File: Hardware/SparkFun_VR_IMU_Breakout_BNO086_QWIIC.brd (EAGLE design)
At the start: 30.5 x 25.4 mm, 97 parts, among them J2 SMD, J3 PTH, J4 SMD, J6 SPI, U2 BNO080, Y1 32.768kHz

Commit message: some more final changes
-added name to revisioner on sch and brd
-moved sch section names to symbol layer, added IMU name
-fixed two DRC errors (angle and stub)
-added more GND vias
-Axis labels - break linear line to show rotation line going over
-Larger SFE flame logo
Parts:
- LOGO4: value SFE_LOGO_FLAME.1_INCH -> SFE_LOGO_FLAME.2_INCH; device SparkFun-Aesthetics:SFE_LOGO_FLAME_.1 -> SparkFun-Aesthetics:SFE_LOGO_FLAME_.2
- moved LOGO4 1.60 mm to (20.4, 12.3)
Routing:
- net GND: vias 10 -> 23
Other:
- board text added: "A. England, P. Lewis"
- board text removed: "A. England"
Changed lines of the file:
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@@
 <setting verticaltext="up"/>
 </settings>
-<grid distance="0.05" unitdist="inch" unit="inch" style="lines" multiple="1" display="yes" altdistance="0.005" altunitdist="inch" altunit="inch"/>
+<grid distance="0.05" unitdist="inch" unit="inch" style="lines" multiple="1" display="yes" altdistance="0.0001" altunitdist="inch" altunit="inch"/>
 <layers>
 <layer number="1" name="Top" color="4" fill="1" visible="yes" active="yes"/>
@@
 <layer number="45" name="Holes" color="7" fill="1" visible="yes" active="yes"/>
 <layer number="46" name="Milling" color="3" fill="1" visible="no" active="yes"/>
-<layer number="47" name="Measures" color="7" fill="1" visible="yes" active="yes"/>
+<layer number="47" name="Measures" color="7" fill="1" visible="no" active="yes"/>
 <layer number="48" name="Document" color="7" fill="1" visible="no" active="yes"/>
 <layer number="49" name="Reference" color="7" fill="1" visible="yes" active="yes"/>
@@
 <layer number="98" name="Guide" color="6" fill="1" visible="no" active="no"/>
 <layer number="99" name="SpiceOrder" color="7" fill="1" visible="no" active="no"/>
-<layer number="100" name="Muster" color="7" fill="1" visible="yes" active="yes"/>
+<layer number="100" name="Muster" color="7" fill="1" visible="no" active="yes"/>
 <layer number="101" name="Patch_Top" color="12" fill="4" visible="no" active="yes"/>
 <layer number="102" name="Vscore" color="7" fill="1" visible="no" active="yes"/>
@@
 <wire x1="4.0132" y1="18.3642" x2="3.3782" y2="18.9992" width="0.1778" layer="22"/>
 <wire x1="3.3782" y1="18.3642" x2="4.0132" y2="18.9992" width="0.1778" layer="22"/>
-<wire x1="3.683" y1="17.145" x2="1.778" y2="17.145" width="0.1778" layer="21"/>
+<wire x1="3.683" y1="17.145" x2="3.159759375" y2="17.145" width="0.1778" layer="21"/>
 <wire x1="3.683" y1="17.145" x2="3.302" y2="17.526" width="0.1778" layer="21"/>
 <wire x1="3.683" y1="17.145" x2="3.302" y2="16.764" width="0.1778" layer="21"/>
@@
 <wire x1="2.667" y1="16.383" x2="2.413" y2="16.51" width="0.1778" layer="21"/>
 <wire x1="2.413" y1="16.51" x2="2.54" y2="16.764" width="0.1778" layer="21"/>
-<wire x1="1.778" y1="19.558" x2="1.778" y2="17.653" width="0.1778" layer="21"/>
+<wire x1="1.778" y1="19.558" x2="1.778" y2="19.034759375" width="0.1778" layer="21"/>
 <wire x1="1.778" y1="19.558" x2="1.397" y2="19.177" width="0.1778" layer="21"/>
 <wire x1="1.778" y1="19.558" x2="2.159" y2="19.177" width="0.1778" layer="21"/>
@@
 <wire x1="3.128778125" y1="19.656828125" x2="3.038975" y2="19.38741875" width="0.1778" layer="21"/>
 <wire x1="3.038975" y1="19.38741875" x2="3.308384375" y2="19.297615625" width="0.1778" layer="21"/>
-<wire x1="1.778" y1="19.558" x2="1.778" y2="17.653" width="0.1778" layer="22"/>
+<wire x1="1.778" y1="19.558" x2="1.778" y2="19.034759375" width="0.1778" layer="22"/>
 <wire x1="1.778" y1="19.558" x2="2.159" y2="19.177" width="0.1778" layer="22"/>
 <wire x1="1.778" y1="19.558" x2="1.397" y2="19.177" width="0.1778" layer="22"/>
@@
 <wire x1="1.016" y1="18.542" x2="1.143" y2="18.288" width="0.1778" layer="22"/>
 <wire x1="1.143" y1="18.288" x2="1.397" y2="18.415" width="0.1778" layer="22"/>
-<wire x1="3.683" y1="17.145" x2="1.778" y2="17.145" width="0.1778" layer="22"/>
+<wire x1="3.683" y1="17.145" x2="3.159759375" y2="17.145" width="0.1778" layer="22"/>
 <wire x1="3.683" y1="17.145" x2="3.302" y2="16.764" width="0.1778" layer="22"/>
 <wire x1="3.683" y1="17.145" x2="3.302" y2="17.526" width="0.1778" layer="22"/>
@@
 <dimension x1="6.35" y1="1.27" x2="6.35" y2="24.13" x3="-11.43" y3="12.7" textsize="1.27" textratio="15" layer="47" dtype="vertical" unit="inch"/>
 <dimension x1="8.89" y1="19.05" x2="8.89" y2="24.13" x3="-1.27" y3="21.59" textsize="1.27" textratio="15" layer="47" dtype="vertical" unit="inch"/>
-<text x="17.78" y="-10.16" size="1.778" layer="51" font="vector">A. England</text>
+<text x="17.78" y="-10.16" size="1.778" layer="51" font="vector">A. England, P. Lewis</text>
 <dimension x1="0" y1="25.4" x2="30.48" y2="25.4" x3="15.24" y3="35.56" textsize="1.27" textratio="15" layer="47" unit="inch"/>
 <text x="47.498" y="44.069" size="1.778" layer="51" font="vector" align="top-left">Soldermask: Red
@@
 <dimension x1="30.48" y1="0" x2="27.559" y2="18.288" x3="38.1" y3="9.144" textsize="1.27" textratio="15" layer="47" dtype="vertical" unit="inch"/>
 <dimension x1="0" y1="0" x2="5.08" y2="12.7" x3="-7.62" y3="6.35" textsize="1.27" textratio="15" layer="47" dtype="vertical" unit="inch"/>
+<wire x1="1.780540625" y1="18.552159375" x2="1.780540625" y2="17.678396875" width="0.1778" layer="21"/>
+<wire x1="1.780540625" y1="18.552159375" x2="1.780540625" y2="17.678396875" width="0.1778" layer="22"/>
+<wire x1="1.8161" y1="17.139921875" x2="2.6898625" y2="17.139921875" width="0.1778" layer="21"/>
+<wire x1="1.8161" y1="17.139921875" x2="2.6898625" y2="17.139921875" width="0.1778" layer="22"/>
 </plain>
 <attributes>
@@
 <attribute name="VALUE" x="13.462" y="16.51" size="0.6096" layer="27" font="vector" ratio="20" rot="R90" align="top-center"/>
 </element>
-<element name="LOGO4" library="SparkFun-Aesthetics" package="SFE_LOGO_FLAME_.1" value="SFE_LOGO_FLAME.1_INCH" x="19.431" y="11.049" smashed="yes"/>
+<element name="LOGO4" library="SparkFun-Aesthetics" package="SFE_LOGO_FLAME_.2" value="SFE_LOGO_FLAME.2_INCH" x="20.40128125" y="12.316459375" smashed="yes"/>
 <element name="LOGO5" library="SparkFun-Aesthetics" package="SFE_LOGO_NAME_FLAME_.1" value="SFE_LOGO_NAME_FLAME.1_INCH" x="15.181578125" y="7.642859375" smashed="yes" rot="MR0"/>
 <element name="PWR" library="SparkFun-LED" package="LED-0603" value="RED" x="27.559" y="18.288" smashed="yes" rot="R270">
@@
 <wire x1="10.16" y1="13.55" x2="10.834" y2="13.55" width="0.1524" layer="1"/>
 <wire x1="13.49" y1="14.4" x2="13.49" y2="13.815" width="0.1524" layer="1"/>
-<wire x1="12.844" y1="12.954" x2="12.84" y2="12.95" width="0.1524" layer="1"/>
 <wire x1="10.16" y1="13.55" x2="8.89" y2="13.55" width="0.1524" layer="1"/>
 <wire x1="8.89" y1="13.55" x2="6.692" y2="13.55" width="0.1524" layer="1"/>
@@
 <wire x1="23.202" y1="6.77" x2="23.241" y2="6.731" width="0.1524" layer="1"/>
 <wire x1="5.9436" y1="6.35" x2="5.9436" y2="8.89" width="0.1524" layer="16"/>
-<wire x1="5.9436" y1="8.89" x2="5.9" y2="9.71" width="0.1524" layer="16"/>
-<wire x1="5.9" y1="9.71" x2="7.62" y2="11.43" width="0.1524" layer="16"/>
 <via x="7.62" y="11.43" extent="1-16" drill="0.3048"/>
 <wire x1="7.62" y1="11.43" x2="8.382" y2="11.43" width="0.1524" layer="1"/>
@@
 <contactref element="J2" pad="2"/>
 <contactref element="J3" pad="2"/>
+<wire x1="5.9436" y1="8.89" x2="5.9436" y2="9.7536" width="0.1524" layer="16"/>
+<wire x1="5.9436" y1="9.7536" x2="7.62" y2="11.43" width="0.1524" layer="16"/>
 </signal>
 <signal name="GND">
@@
 <contactref element="J2" pad="1"/>
 <contactref element="J3" pad="1"/>
+<via x="22.733" y="10.16" extent="1-16" drill="0.3048"/>
+<via x="21.082" y="9.398" extent="1-16" drill="0.3048"/>
+<via x="19.431" y="9.652" extent="1-16" drill="0.3048"/>
+<via x="21.082" y="5.715" extent="1-16" drill="0.3048"/>
+<via x="19.431" y="5.715" extent="1-16" drill="0.3048"/>
+<via x="7.09168125" y="17.205959375" extent="1-16" drill="0.3048"/>
+<via x="5.68198125" y="17.3482" extent="1-16" drill="0.3048"/>
+<via x="3.79221875" y="17.69871875" extent="1-16" drill="0.3048"/>
+<via x="10.2209625" y="21.493478125" extent="1-16" drill="0.3048"/>
+<via x="25.27808125" y="21.4376" extent="1-16" drill="0.3048"/>
+<via x="9.667240625" y="5.323840625" extent="1-16" drill="0.3048"/>
+<via x="7.680959375" y="4.68121875" extent="1-16" drill="0.3048"/>
+<via x="4.97331875" y="4.132578125" extent="1-16" drill="0.3048"/>
 </signal>
 <signal name="CAP">
@@
 <wire x1="9.691" y1="11.85" x2="8.636" y2="10.795" width="0.1524" layer="1"/>
 <wire x1="8.636" y1="10.795" x2="6.985" y2="10.795" width="0.1524" layer="1"/>
-<wire x1="6.985" y1="10.795" x2="3.81" y2="7.62" width="0.1524" layer="1"/>
+<wire x1="6.985" y1="10.795" x2="6.35" y2="10.16" width="0.1524" layer="1"/>
+<wire x1="6.35" y1="10.16" x2="3.81" y2="7.62" width="0.1524" layer="1"/>
 <wire x1="3.81" y1="7.62" x2="1.27" y2="7.62" width="0.1524" layer="1"/>
 </signal>
@@
 <wire x1="21.59" y1="24.13" x2="20.32" y2="22.86" width="0.1524" layer="16"/>
 <wire x1="5.08" y1="5.461" x2="5.461" y2="5.08" width="0.1524" layer="16"/>
-<wire x1="5.08" y1="21.59" x2="5.08" y2="5.461" width="0.1524" layer="16"/>
-<wire x1="20.32" y1="22.86" x2="6.35" y2="22.86" width="0.1524" layer="16"/>
-<wire x1="6.35" y1="22.86" x2="5.08" y2="21.59" width="0.1524" layer="16"/>
+<wire x1="5.08" y1="21.122640625" x2="5.08" y2="5.461" width="0.1524" layer="16"/>
+<wire x1="20.32" y1="22.86" x2="6.817359375" y2="22.86" width="0.1524" layer="16"/>
+<wire x1="6.817359375" y1="22.86" x2="5.08" y2="21.122640625" width="0.1524" layer="16"/>
 <contactref element="J8" pad="2"/>
 <wire x1="6.35" y1="5.08" x2="6.35" y2="1.27" width="0.1524" layer="16"/>
@@
 <wire x1="16.99" y1="9.553" x2="17.018" y2="9.525" width="0.1524" layer="1"/>
 <via x="17.018" y="9.525" extent="1-16" drill="0.3048"/>
-<wire x1="17.018" y1="9.525" x2="17.018" y2="5.842" width="0.1524" layer="16"/>
-<wire x1="17.018" y1="5.842" x2="17.78" y2="5.08" width="0.1524" layer="16"/>
-<via x="17.78" y="5.08" extent="1-16" drill="0.3048"/>
-<wire x1="17.78" y1="5.08" x2="20.32" y2="5.08" width="0.1524" layer="1"/>
-<wire x1="20.32" y1="5.08" x2="24.13" y2="1.27" width="0.1524" layer="1"/>
+<wire x1="17.018" y1="9.525" x2="17.018" y2="5.798821875" width="0.1524" layer="16"/>
+<wire x1="17.018" y1="5.798821875" x2="17.78" y2="5.036821875" width="0.1524" layer="16"/>
+<via x="17.78" y="5.036821875" extent="1-16" drill="0.3048"/>
+<wire x1="17.78" y1="5.036821875" x2="20.363178125" y2="5.036821875" width="0.1524" layer="1"/>
+<wire x1="20.363178125" y1="5.036821875" x2="24.13" y2="1.27" width="0.1524" layer="1"/>
 </signal>
 <signal name="SCL/SCK/RX">

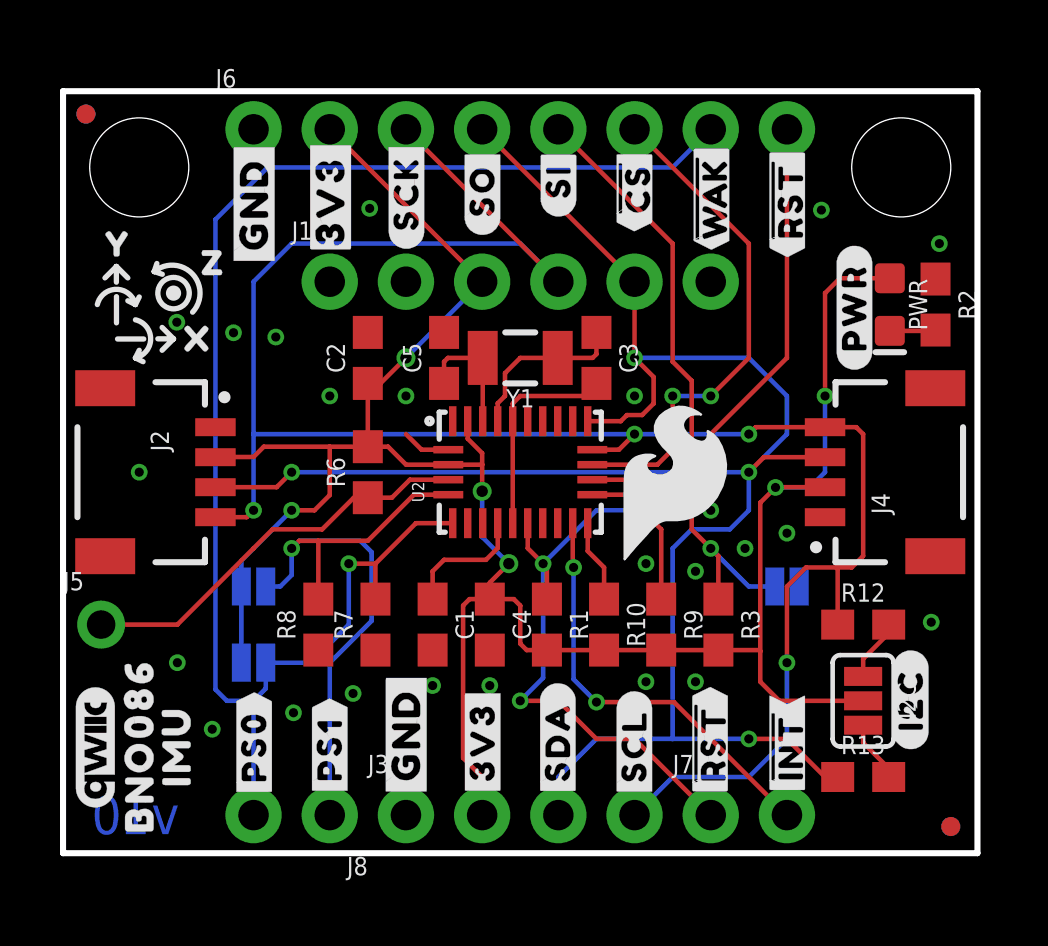
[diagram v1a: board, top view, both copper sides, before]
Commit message: 3V3 net to thicker trace and more
-upped 3v3 trace to 20mil
-nudges some vias/traces for better GND flow
-added more gnd vias
-reduced GND pour isolates from 12 to 10
-I2C pullup jumper changes to NC trace
-updated IC to 086, in temp library for now
-added Power LED jumper
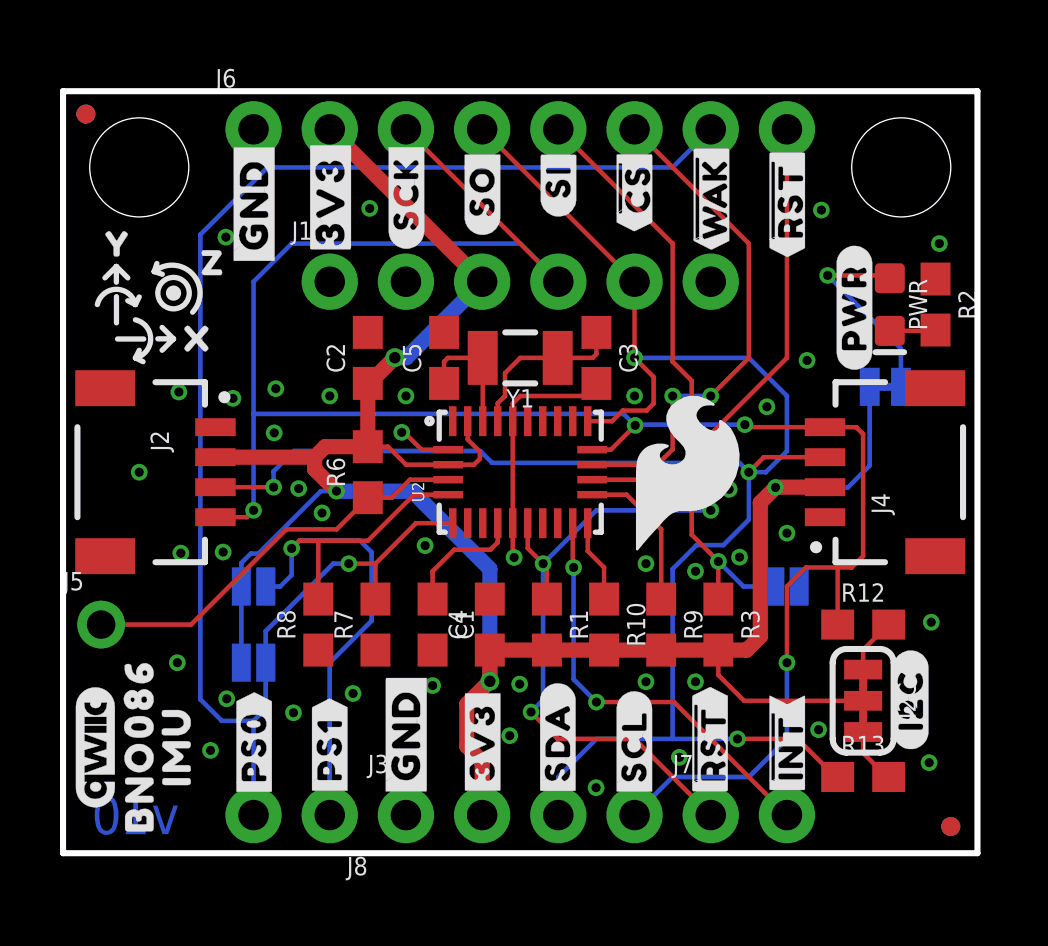
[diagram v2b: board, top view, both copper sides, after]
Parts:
- added LED: (no value), SparkFun-Jumpers:SMT-JUMPER_2_NC_TRACE_SILK
- added U$26: (no value), output:#LED#0
- I2C: device SparkFun-Jumpers:SMT-JUMPER_3_2-NC_PASTE_SILK -> SparkFun-Jumpers:SMT-JUMPER_3_2-NC_TRACE_SILK
- U2: value BNO080 -> BNO086; device SparkFun-IC-Special-Function:LGA-28 -> bno086:LGA-28
- moved LOGO4 0.53 mm to (20.8, 12.6)
- turned C4 to 90 degrees
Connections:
- new net N$4: LED.2, PWR.A
- net 3.3V: now also LED.1; no longer PWR.A
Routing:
- net N$4: track 0.00 -> 6.83 mm, vias 0 -> 1
- net 3.3V: track 80.4 -> 78.2 mm, vias 6 -> 4
- net GND: track 8.68 -> 9.84 mm, vias 23 -> 41
- net SDA/MISO/TX: track 65.7 -> 66.7 mm
- net PS0/WAKE: track 50.6 -> 51.2 mm
